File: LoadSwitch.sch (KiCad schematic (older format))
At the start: 20 parts, among them IC1 LTC4359, P1 CONN_01X03, P2 CONN_01X03, P3 CONN_01X02, P4 CONN_01X02, Q1 FDMS86101, Q2 FDMS86101

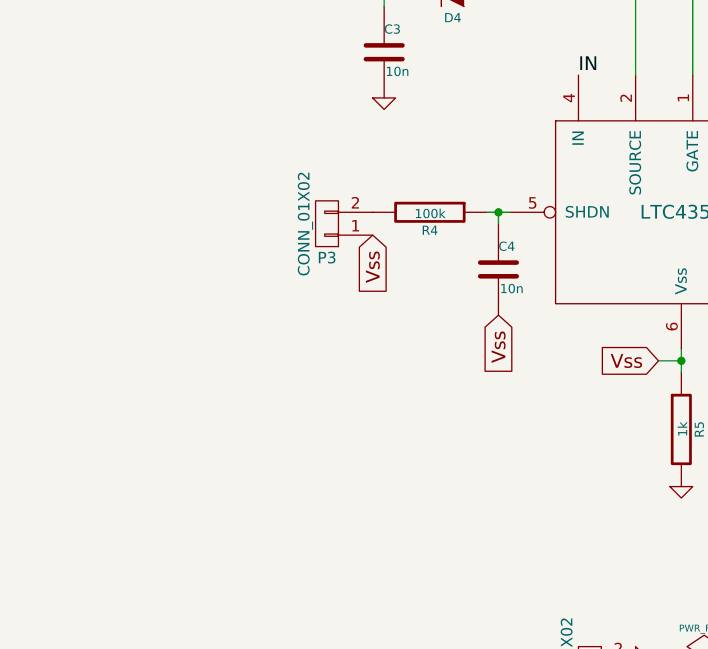
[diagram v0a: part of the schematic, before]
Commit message: Korrekte Ansteuerung des SHDN pins
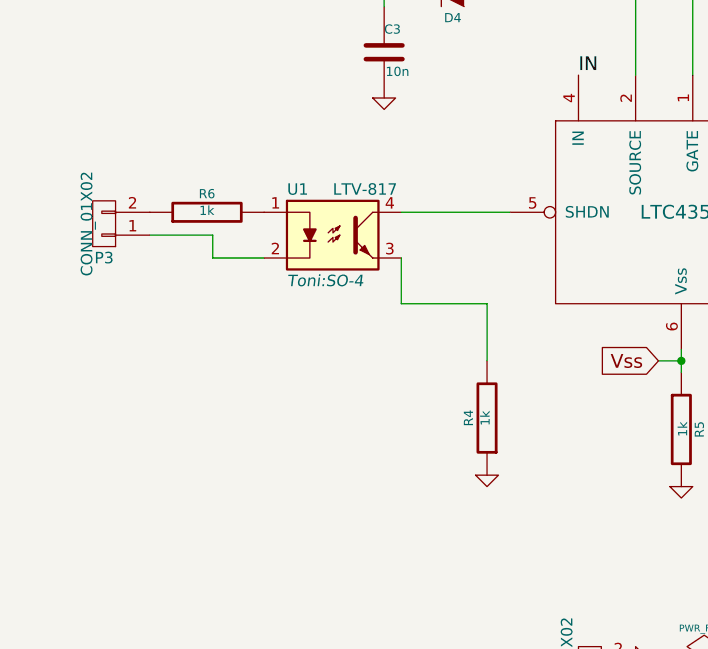
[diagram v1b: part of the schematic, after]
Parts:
- removed C4: 10n, Capacitors_SMD:C_0805, symbol C-RESCUE-LoadSwitch
- added R6: 1k, Resistors_SMD:R_0603_HandSoldering, symbol R-RESCUE-LoadSwitch
- added U1: LTV-817, Toni:SO-4, symbol LTV-817
- R4: value 100k -> 1k
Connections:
- net GND: now also R4.1
- net Vss: no longer P3.1 (P1)
- net at IC1.5 (SHDN): now also U1.4; no longer R4.1
- net at P3.2 (P2): now also R6.1; no longer R4.2
- new net: P3.1 (P1), U1.2
- new net: R4.2, U1.3
- new net: R6.2, U1.1
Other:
- moved on the sheet: P3, R4
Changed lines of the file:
@@
 L CONN_01X02 P3
 U 1 1 56499CAE
-P 2500 4200
-F 0 "P3" H 2500 4350 50  0000 C CNN
-F 1 "CONN_01X02" V 2600 4200 50  0000 C CNN
-F 2 "Pin_Headers:Pin_Header_Angled_1x03" H 2500 4200 60  0001 C CNN
-F 3 "" H 2500 4200 60  0000 C CNN
-	1    2500 4200
+P 1525 4200
+F 0 "P3" H 1525 4350 50  0000 C CNN
+F 1 "CONN_01X02" V 1600 4200 50  0000 C CNN
+F 2 "Pin_Headers:Pin_Header_Angled_1x03" H 1525 4200 60  0001 C CNN
+F 3 "" H 1525 4200 60  0000 C CNN
+	1    1525 4200
 	-1   0    0    1
 $EndComp
@@
 L R-RESCUE-LoadSwitch R4
 U 1 1 56499D33
-P 2950 4150
-F 0 "R4" V 3030 4150 40  0000 C CNN
-F 1 "100k" V 2957 4151 40  0000 C CNN
-F 2 "Resistors_SMD:R_0603_HandSoldering" V 2880 4150 30  0001 C CNN
-F 3 "" H 2950 4150 30  0000 C CNN
-	1    2950 4150
-	0    1    1    0
+P 3200 5050
+F 0 "R4" V 3280 5050 40  0000 C CNN
+F 1 "1k" V 3207 5051 40  0000 C CNN
+F 2 "Resistors_SMD:R_0603_HandSoldering" V 3130 5050 30  0001 C CNN
+F 3 "" H 3200 5050 30  0000 C CNN
+	1    3200 5050
+	-1   0    0    1
 $EndComp
-Text GLabel 2700 4250 3    60   Input ~ 0
-Vss
-Wire Wire Line
-	3200 4150 3300 4150
-$Comp
-L C-RESCUE-LoadSwitch C4
-U 1 1 56499EAB
-P 3250 4400
-F 0 "C4" H 3250 4500 40  0000 L CNN
-F 1 "10n" H 3256 4315 40  0000 L CNN
-F 2 "Capacitors_SMD:C_0805" H 3288 4250 30  0001 C CNN
-F 3 "" H 3250 4400 60  0000 C CNN
-	1    3250 4400
-	1    0    0    -1
-$EndComp
-Wire Wire Line
-	3250 4200 3250 4150
-Connection ~ 3250 4150
-Text GLabel 3250 4600 3    60   Input ~ 0
-Vss
 $Comp
 L CONN_01X02 P4
@@
 	4050 4800 3950 4800
 Connection ~ 4050 4800
+$Comp
+L GND-RESCUE-LoadSwitch #PWR08
+U 1 1 565D6957
+P 3200 5300
+F 0 "#PWR08" H 3200 5300 30  0001 C CNN
+F 1 "GND" H 3200 5230 30  0001 C CNN
+F 2 "" H 3200 5300 60  0000 C CNN
+F 3 "" H 3200 5300 60  0000 C CNN
+	1    3200 5300
+	1    0    0    -1
+$EndComp
+Wire Wire Line
+	2825 4150 3300 4150
+$Comp
+L LTV-817 U1
+U 1 1 565D6B0A
+P 2525 4250
+F 0 "U1" H 2325 4450 50  0000 L CNN
+F 1 "LTV-817" H 2525 4450 50  0000 L CNN
+F 2 "Toni:SO-4" H 2325 4050 50  0000 L CIN
+F 3 "" H 2525 4150 50  0000 L CNN
+	1    2525 4250
+	1    0    0    -1
+$EndComp
+Wire Wire Line
+	2825 4350 2825 4550
+Wire Wire Line
+	2825 4550 3200 4550
+Wire Wire Line
+	3200 4550 3200 4800
+$Comp
+L R-RESCUE-LoadSwitch R6
+U 1 1 565D6F3D
+P 1975 4150
+F 0 "R6" V 2055 4150 40  0000 C CNN
+F 1 "1k" V 1982 4151 40  0000 C CNN
+F 2 "Resistors_SMD:R_0603_HandSoldering" V 1905 4150 30  0001 C CNN
+F 3 "" H 1975 4150 30  0000 C CNN
+	1    1975 4150
+	0    -1   -1   0
+$EndComp
+Wire Wire Line
+	1725 4250 2000 4250
+Wire Wire Line
+	2000 4250 2000 4350
+Wire Wire Line
+	2000 4350 2225 4350
 $EndSCHEMATC
